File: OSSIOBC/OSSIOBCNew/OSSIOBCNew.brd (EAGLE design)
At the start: 94 x 94 mm, 158 parts, among them Q2 NX-3215, U1 PCA9548APWR, U10 MAX6369, U11 OPA4347, U13 SN65HVD11QD, U14 LTC4411, U15 MCP1700_SOT23, U16 DS3231-L, U17 FM24V02-G, U18 TMP101, U19 24LC256-8LEAD, U2 ADG708, U20 LTC4411, U21 SN74LVC8T245PWR, U23 ADXRS450SOIC, U3 MAX890L, U4 OPA4347, U5 MSP430F1611, U6 OPA4347, U7 TPS3838, U8 ADG708, U9 ADR121, X1 ESQ-126-38-G-D, X2 JTAG10PINMINI-H, X3 MOLEX-22-05-7045, X5 P-PAD-S, X6 P-PAD-S

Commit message: schematics renumbered
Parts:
- removed C42: 10uF, LDO Tantal 16V, OSSI:C1206(3216)-A
- removed U23: ADXRS450SOIC, OSSI:SOIC-16CAV
- added C35: 100nF, OSSI:C0603(1608)
- added U12: TMP101, OSSI:SOT23-6DBV
- C1: value 1uF -> 100nF
- C13, C14: value 12.5pF -> 100nF
- C20, C22, C23: value 100nF -> 1uF 0805; device OSSI:C0603(1608) -> OSSI:C0805(2012)
- C29: value 1uF 0805 -> 4.7uF, 1210; device OSSI:C0805(2012) -> OSSI:C1206-GCM31
- C30: value 1uF 0805 -> 10uF,3225; device OSSI:C0805(2012) -> OSSI:C1210-GCM32
- C31: value 100nF -> 12.5pF
- C32: value 1uF 0805 -> 12.5pF; device OSSI:C0805(2012) -> OSSI:C0603(1608)
- C34: value 10uF, LDO Tantal 16V -> 100nF; device OSSI:C1206(3216)-A -> OSSI:C0603(1608)
- C37: value 10uF,3225 -> 100nF; device OSSI:C1210-GCM32 -> OSSI:C0603(1608)
- C38: value 4.7uF, 1210 -> 1uF; device OSSI:C1206-GCM31 -> OSSI:C0603(1608)
- C40, C41: value 100nF -> 10uF, LDO Tantal 16V; device OSSI:C0603(1608) -> OSSI:C1206(3216)-A
- R1: value TBD -> 10k
- R10, R11, R62: value 10k -> 100k
- R12, R13: value 33k -> 100k
- R18, R2, R3, R4, R6, R7, R9: value 100k -> 10k
- R19, R41: value 100k -> 250
- R20, R43: value 100k -> 470k
- R21, R30, R31, R38: value 10k -> 250
- R22, R23, R26, R28, R29: value 250 -> 1.5k
- R27: value 250 -> 100k
- R32: value 250 -> 4.7k
- R33: value 250 -> 470k
- R34: value 4.7k -> 470k
- R35: value 120, DNP -> 33k
- R36, R39, R68, R71: value 10k -> 4.7k
- R37: value 10k -> 120, DNP
- R40: value 10k -> 33k
- R42, R69, R70: value 1.5k -> 4.7k
- R44: value 470k -> 4.7k
- R45: value 4.7k -> 100k
- R46: value 1.5k -> 470k
- R47, R48, R49: value 1.5k -> 100k
- R52, R57: value 4.7k -> 1.5k
- R54: value 1.5k -> 10k
- R56: value 10k -> 1.5k
- R58, R60, R65: value 470k -> 10k
- R59, R61, R8: value 4.7k -> 10k
- R63: value 4.7k -> 250
- R64: value 470k -> 250
- R66: value 4.7k -> 300k
- R67: value 300k -> 10k
- R72, R73: value 10k -> 0
- R74: value 100k -> TBD
- R76, R77: value 0 -> 100k
- U1: value PCA9548APWR -> OPA4347; device OSSI:TSSOP-24-PW -> OSSI:TSSOP14-PW
- U10: value MAX6369 -> ADXRS450SOIC; device OSSI:SOT23-8 -> OSSI:SOIC-16CAV
- U11: value OPA4347 -> FM24V02-G; device OSSI:TSSOP14-PW -> OSSI:SO8
- U14: value LTC4411 -> PCA9548APWR; device OSSI:TSOT23-5 -> OSSI:TSSOP-24-PW
- U15: value MCP1700_SOT23 -> SN74LVC8T245PWR; device OSSI:SOT23 -> OSSI:PW_R-PDSO-G24
- U16: value DS3231-L -> LTC4411; device OSSI:SO16L -> OSSI:TSOT23-5
- U17: value FM24V02-G -> MSP430F1611; device OSSI:SO8 -> OSSI:PM/PAG64
- U18: value TMP101 -> MAX6369; device OSSI:SOT23-6DBV -> OSSI:SOT23-8
- U19: value 24LC256-8LEAD -> TPS3838; device OSSI:SO08-208 -> OSSI:SOT23-5DBV
- U20: value LTC4411 -> MAX890L; device OSSI:TSOT23-5 -> OSSI:SO8
- U21: value SN74LVC8T245PWR -> MCP1700_SOT23; device OSSI:PW_R-PDSO-G24 -> OSSI:SOT23
- U3: value MAX890L -> OPA4347; device OSSI:SO8 -> OSSI:TSSOP14-PW
- U4: value OPA4347 -> ADR121; device OSSI:TSSOP14-PW -> OSSI:TSOT-6UJ-6
- U5: value MSP430F1611 -> ADG708; device OSSI:PM/PAG64 -> OSSI:TSSOP16-RU
- U7: value TPS3838 -> DS3231-L; device OSSI:SOT23-5DBV -> OSSI:SO16L
- U8: value ADG708 -> 24LC256-8LEAD; device OSSI:TSSOP16-RU -> OSSI:SO08-208
- U9: value ADR121 -> LTC4411; device OSSI:TSOT-6UJ-6 -> OSSI:TSOT23-5
- X2: value JTAG10PINMINI-H -> MOLEX-22-05-7045; device OSSI:M50-3200545 -> OSSI:22-05-7045
- X3: value MOLEX-22-05-7045 -> (none); device OSSI:22-05-7045 -> OSSI:1X03
- X4: value (none) -> P-PAD-S; device OSSI:1X03 -> OSSI:P-PAD-S
- X6: value P-PAD-S -> JTAG10PINMINI-H; device OSSI:P-PAD-S -> OSSI:M50-3200545
- moved R74 82.4 mm to (67.8, 85.0), turned to 0 degrees
- moved R20 81.5 mm to (53.3, 6.02), turned to 180 degrees
- moved U16 77.4 mm to (62.2, 90.0), turned to 270 degrees
- moved H1 76.0 mm to (85.0, 85.0)
- moved H2 76.0 mm to (85.0, 9.00)
- moved H3 76.0 mm to (9.00, 9.00)
- moved H4 76.0 mm to (9.00, 85.0)
- moved R41 73.8 mm to (29.0, 18.8), turned to 270 degrees
- moved U9 71.9 mm to (46.1, 6.50)
- moved U7 70.5 mm to (55.8, 12.9), turned to 0 degrees
- moved U19 64.0 mm to (20.5, 74.0), turned to 270 degrees
- moved R52 63.9 mm to (16.1, 54.0), flipped to the top, turned to 90 degrees
- moved C2 63.9 mm to (71.0, 52.2)
- moved R53 62.5 mm to (17.6, 52.0), flipped to the top, turned to 90 degrees
- moved R38 61.2 mm to (30.5, 17.0), turned to 270 degrees
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- renumbered Q2 to Q1, TR2 to TR1
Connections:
- net /RE: now also R40.1; no longer R12.1
- net 3.3VOBC: now also C14.2, C20.1, C26.1, C34.1, C36.1, C37.1, C4.1, C41.1, C9.1, R34.2, R40.2, R46.2, R48.2, R54.2, R59.2, R65.2, R66.1, R67.2, R77.2, U1.4, U14.24, U15.1, U17.1, U17.64, U18.4, U18.5, U18.6, U18.8, U19.5, U21.2, U3.4, U4.3, U5.13, U5.2, U9.P$1, X6.4; no longer C12.1, C17.2, C2.1, C27.1, C30.1, C42.1, C6.1, C7.1, C8.1, R12.2, R2.2, R30.2, R31.2, R4.2, R44.2, R56.2, R58.2, R67.1, R73.2, U1.24, U10.4, U10.5, U10.8, U11.4, U14.P$1, U15.2, U21.1, U23.6, U4.4, U5.1, U5.64, U7.5, U8.13, U8.2, U9.3, X2.4
- net 3.3VOBC_I2C: now also C24.1, C25.1, R20.2, R33.1, R58.2, R61.2, U11.1, U11.8, U12.4, U7.2, U8.8, U9.P$5; no longer C20.1, C21.1, R5.2, R64.2, R65.1, R72.2, U14.P$5, U16.2, U17.1, U17.8, U18.4, U19.8
- net A: now also R37.2, X2.2; no longer R35.2, X3.2
- net ADC0: now also C12.1, R9.1, U17.59; no longer C5.1, R10.1, U5.59
- net ADC1: now also C17.1, R18.1, U17.60; no longer C9.1, R11.1, U5.60
- net ANT_DEPLOY1: now also R70.1; no longer R45.1
- net ANT_DEPLOY2: now also R69.1; no longer R52.1
- net B: now also R37.1, X2.3; no longer R35.1, X3.3
- net BAT_-CHRG: now also U15.18; no longer U21.18
- net BAT_-CHRG_IN: now also R53.2, U17.17; no longer R48.2, U5.17
- net BAT_-FAULT: now also U15.17; no longer U21.17
- net BAT_-FAULT_IN: now also R52.2, U17.16; no longer R49.2, U5.16
- net BAT_-ON: now also U15.20; no longer U21.20
- net BAT_-ON_IN: now also R56.2, U17.19; no longer R46.2, U5.19
- net BAT_TEMP: now also R2.2; no longer R68.2
- net BEACON_-FAULT: now also R42.1, R43.1; no longer R58.1, R59.1
- net BEACON_-FAULT_IN: now also R42.2, U17.22; no longer R59.2, U5.22
- net BEACON_OFF: now also R28.1; no longer R54.1
- net BEACON_OFF_OUT: now also R28.2, U17.38; no longer R54.2, U5.38
- net BEACON_SCL: now also U14.7; no longer U1.7
- net BEACON_SDA: now also U14.6; no longer U1.6
- net BUS_CS: now also R4.2; no longer R40.2
- net COMMS_-FAULT: now also R32.1, R34.1; no longer R60.1, R61.1
- net COMMS_-FAULT_IN: now also R32.2, U17.21; no longer R61.2, U5.21
- net COMMS_OFF: now also R26.1; no longer R55.1
- net COMMS_OFF_OUT: now also R26.2, U17.37; no longer R55.2, U5.37
- net COMMS_SCL: now also U14.5; no longer U1.5
- net COMMS_SDA: now also U14.4; no longer U1.4
- net DE: now also R35.2, U17.48; no longer R13.2, U5.48
- net GND: now also C13.1, C14.1, C17.2, C21.1, C29.P$2, C30.P$2, C31.2, C33.2, C35.2, C37.2, C38.2, R10.1, R12.1, R14.1, R16.1, R27.2, R35.1, R45.2, R49.2, R74.1, R76.1, U1.11, U10.10, U10.11, U10.12, U10.13, U10.3, U10.7, U11.2, U11.3, U11.4, U11.7, U12.2, U12.5, U14.1, U14.12, U14.2, U14.21, U15.11, U15.12, U15.13, U15.14, U15.2, U16.P$2, U17.11, U17.53, U17.62, U17.63, U20.4, U21.1, U3.11, U4.2, U5.10, U5.12, U5.14, U5.3, U5.9, U7.10, U7.11, U7.12, U7.13, U7.5, U7.6, U7.7, U7.8, U7.9, U8.1, U8.2, U8.4, U8.7, U9.P$2, X2.4, X3.3, X6.9; no longer C13.2, C14.2, C17.1, C21.2, C29.2, C30.2, C31.1, C33.1, C37.P$2, C38.P$2, C41.2, R1.1, R13.1, R15.1, R17.1, R19.1, R20.2, R3.1, R41.2, R74.2, R9.1, U1.1, U1.12, U1.2, U1.21, U11.11, U14.P$2, U15.1, U16.10, U16.11, U16.12, U16.13, U16.5, U16.6, U16.7, U16.8, U16.9, U17.2, U17.3, U17.4, U17.7, U18.5, U19.3, U19.4, U19.7, U2.10, U2.11, U2.12, U2.9, U20.P$2, U21.11, U21.12, U21.13, U21.14, U21.2, U23.10, U23.11, U23.12, U23.13, U23.2, U23.3, U23.7, U3.4, U4.11, U5.53, U5.62, U5.63, U7.1, U7.2, U8.14, U9.2, X2.9, X3.4, X4.3
- net GYRO_-CS: now also U10.4, U17.44; no longer U23.4, U5.44
- net GYRO_SCLK: now also U10.16, U17.47; no longer U23.16, U5.47
- net GYRO_SI: now also U10.15, U17.45; no longer U23.15, U5.45
- net GYRO_SO: now also U10.5, U17.46; no longer U23.5, U5.46
- net I2C_-RST: now also R48.1, U14.3, U17.28; no longer R4.1, U1.3, U5.28
- net I2C_SCL: now also R64.1, R67.1, U14.22; no longer R26.1, R30.1, U1.22
- net I2C_SCL_TP: now also R64.2, U17.31, X3.2; no longer R26.2, U5.31, X4.2
- net I2C_SDA: now also R63.1, R65.1, U14.23; no longer R27.1, R31.1, U1.23
- net I2C_SDA_TP: now also R63.2, U17.29, X3.1; no longer R27.2, U5.29, X4.1
- net IO_-OE: now also R62.1, U15.22, U17.24; no longer R43.1, U21.22, U5.24
- net LED_-FAULT: now also R46.1; no longer R57.1
- net LED_-FAULT_IN: now also R44.2, U17.23; no longer R57.2, U5.23
- net LED_OFF: now also R29.1; no longer R53.1
- net LED_OFF_OUT: now also R29.2, U17.39; no longer R53.2, U5.39
- net LED_SCL: now also U14.9; no longer U1.9
- net LED_SDA: now also U14.8; no longer U1.8
- net MUX_A0: now also R73.2, U5.1; no longer R76.2, U8.1
- net MUX_A1: now also R72.2, U5.16; no longer R77.2, U8.16
- net MUX_A2: now also U17.51, U5.15; no longer U5.51, U8.15
- net N$1: now also U17.12, U18.1; no longer U10.1, U5.12
- net N$10: now also R74.2, U20.5; no longer R1.2, U3.5
- net N$11: now also U5.4, U6.13, U6.14; no longer U2.4, U4.13, U4.14
- net N$12: now also U2.7, U3.1, U3.2; no longer U6.1, U6.2, U8.7
- net N$13: now also C33.1, U17.7; no longer C10.1, U5.7
- net N$14: now also R39.2; no longer R34.2
- net N$15: now also R21.2, U7.16; no longer R33.2, U16.16
- net N$16: now also R54.1, U14.15, U14.16, U14.17, U14.18, U14.19, U14.20; no longer R73.1, U1.15, U1.16, U1.17, U1.18, U1.19, U1.20
- net N$17: now also U17.57, X6.7; no longer U5.57, X2.7
- net N$18: now also U17.56, X6.5; no longer U5.56, X2.5
- net N$19: now also U17.55, X6.3; no longer U5.55, X2.3
- net N$2: now also R16.2, R17.1, U6.3; no longer R7.1, R9.2, U4.3
- net N$20: now also U17.54, X6.1; no longer U5.54, X2.1
- net N$21: now also U2.6, U3.6, U3.7; no longer U6.6, U6.7, U8.6
- net N$22: now also R36.2; no longer R63.2
- net N$23: now also R71.1, X6.10; no longer R8.1, X2.10
- net N$24: now also R14.2, R15.1, U6.5; no longer R14.1, R15.2, U4.5
- net N$25: now also R12.2, R13.1, U6.10; no longer R16.1, R17.2, U4.10
- net N$26: now also R10.2, R11.1, U6.12; no longer R18.1, R19.2, U4.12
- net N$27: now also R18.2, U5.8; no longer R11.2, U2.8
- net N$28: now also U2.5, U3.8, U3.9; no longer U6.8, U6.9, U8.5
- net N$29: now also R9.2, U2.8; no longer R10.2, U8.8
- net N$3: now also U5.7, U6.1, U6.2; no longer U2.7, U4.1, U4.2
- net N$30: now also U2.4, U3.13, U3.14; no longer U6.13, U6.14, U8.4
- net N$31: now also U1.1, U1.2, U2.12; no longer U11.1, U11.2, U8.12
- net N$32: now also R68.2, U17.13; no longer R66.2, U5.13
- net N$33: now also C23.1, U10.1; no longer C32.1, U23.1
- net N$34: now also R24.2, U8.5; no longer R29.2, U19.5
- net N$35: now also R25.2, U8.6; no longer R28.2, U19.6
- net N$36: now also R30.2, U11.5; no longer R25.2, U17.5
- net N$37: now also R70.2, U17.43; no longer R45.2, U5.43
- net N$38: now also R69.2, U17.42; no longer R52.2, U5.42
- net N$39: now also R31.2, U11.6; no longer R24.2, U17.6
- net N$4: now also R45.1, R47.2; no longer R41.1, R6.2
- net N$40: now also R38.2, U12.6; no longer R22.2, U18.6
- net N$41: now also R41.2, U12.1; no longer R23.2, U18.1
- net N$42: now also R66.2, U17.25; no longer R67.2, U5.25
- net N$43: now also C27.1, X2.1; no longer C36.1, X3.1
- net N$44: now also U1.8, U1.9, U2.10; no longer U11.8, U11.9, U8.10
- net N$45: now also U1.13, U1.14, U2.9; no longer U11.13, U11.14, U8.9
- net N$46: now also C22.1, U10.14; no longer C29.1, U23.14
- net N$47: now also C1.1, R1.1, U1.12; no longer C41.1, R71.1, U11.12
- net N$48: now also C2.1, R2.1, U1.10; no longer C40.1, R68.1, U11.10
- net N$49: now also R53.1, U15.6; no longer R48.1, U21.6
- net N$5: now also C32.1, U17.8; no longer C13.1, U5.8
- net N$50: now also R52.1, U15.7; no longer R49.1, U21.7
- net N$51: now also C10.1, R8.1, U3.3; no longer C22.1, R21.1, U6.3
- net N$52: now also C8.1, R7.1, U3.5; no longer C23.1, R36.1, U6.5
- net N$53: now also C7.1, R6.1, U3.10; no longer C24.1, R37.1, U6.10
- net N$54: now also C6.1, R5.1, U3.12; no longer C25.1, R38.1, U6.12
- net N$55: now also C3.1, R3.1, U1.3; no longer C26.1, R39.1, U11.3
- net N$56: now also R51.1, U15.8; no longer R50.1, U21.8
- net N$57: now also R50.1, U15.9; no longer R51.1, U21.9
- net N$58: now also C5.1, R4.1, U1.5; no longer C39.1, R40.1, U11.5
- net N$59: now also C41.2; no longer C42.2
- net N$6: now also C31.1, U17.9; no longer C14.1, U5.9
- net N$60: now also U17.33; no longer U5.33
- net N$61: now also U17.32, X4.1; no longer U5.32, X6.1
- net N$62: now also R73.1, U17.49; no longer R76.1, U5.49
- net N$64: now also R72.1, U17.50; no longer R77.1, U5.50
- net N$65: now also U7.14; no longer U16.14
- net N$666: now also C39.1, C40.1, U20.6, U20.7, U21.3; no longer C3.1, C34.1, U15.3, U3.6, U3.7
- net N$7: now also R19.2, U7.15; no longer R32.2, U16.15
- net N$70: now also R55.1, U15.5; no longer R47.1, U21.5
- net N$71: now also R56.1, U15.4; no longer R46.1, U21.4
- net N$72: now also R57.1, U15.3; no longer R42.1, U21.3
- net N$8: now also U5.6, U6.6, U6.7; no longer U2.6, U4.6, U4.7
- net N$82: now also U10.8; no longer U23.8
- net N$9: now also U5.5, U6.8, U6.9; no longer U2.5, U4.8, U4.9
- net N$90: now also C21.2, U10.9; no longer C31.2, U23.9
- net OBC_-FAULT: now also U20.8; no longer U3.8
- net OBC_I2C_OFF: now also R27.1, U17.30, U9.P$3; no longer R74.1, U14.P$3, U5.30
- net OBC_OFF: now also C38.1, R76.2, U20.3; no longer C1.1, R3.2, U3.3
- net OBC_SCL: now also R21.1, R25.1, R31.1, R41.1, R58.1, U14.14; no longer R23.1, R24.1, R28.1, R33.1, R72.1, U1.14
- net OBC_SDA: now also R19.1, R24.1, R30.1, R38.1, R61.1, U14.13; no longer R22.1, R25.1, R29.1, R32.1, R5.1, U1.13
- net OBC_WT_RST: now also C35.1, U18.7, U19.3; no longer C4.1, U10.7, U7.3
- net PANELTEMP_SCL: now also R59.1, U14.11; no longer R56.1, U1.11
- net PANELTEMP_SDA: now also R60.1, U14.10; no longer R62.1, U1.10
- net RESETOBC: now also R71.2, R77.1, U17.58, U19.4; no longer R2.1, R8.2, U5.58, U7.4
- net RTC_-INT: now also R20.1, U17.26, U7.3; no longer R64.1, U16.3, U5.26
- net RXD1: now also R39.1, U17.35; no longer R34.1, U5.35
- net SCCHG_EN: now also R23.1; no longer R69.1
- net SCCHG_EN_OUT: now also R23.2, U17.41; no longer R69.2, U5.41
- net SCOUT_-PG: now also U15.15; no longer U21.15
- net SCOUT_-PG_IN: now also R50.2, U17.14; no longer R51.2, U5.14
- net SCOUT_EN: now also R22.1; no longer R70.1
- net SCOUT_EN_OUT: now also R22.2, U17.40; no longer R70.2, U5.40
- net SC_-ON: now also U15.19; no longer U21.19
- net SC_-ON_IN: now also R55.2, U17.18; no longer R47.2, U5.18
- net SC_-PFO: now also U15.16; no longer U21.16
- net SC_-PFO_IN: now also R51.2, U17.15; no longer R50.2, U5.15
- net SOLAR_-ON: now also U15.21; no longer U21.21
- net SOLAR_-ON_IN: now also R57.2, U17.20; no longer R42.2, U5.20
- net SOLAR_CS1: now also R8.2; no longer R21.2
- net SOLAR_CS2: now also R7.2; no longer R36.2
- net SOLAR_CS3: now also R6.2; no longer R37.2
- net SOLAR_CS4: now also R5.2; no longer R38.2
- net SOLAR_CS5: now also R3.2; no longer R39.2
- net STATUS_LED: now also R68.1; no longer R66.1
- net SUN_IN: now also U1.6, U1.7, U2.11; no longer U11.6, U11.7, U8.11
- net SUPERCAP_TEMP: now also R1.2; no longer R71.2
- net TEMP_-ALERT: now also R33.2, U12.3, U17.27; no longer R65.2, U18.3, U5.27
- net TXD1: now also R36.1, U17.34; no longer R63.1, U5.34
- net VBAT: now also R13.2; no longer R16.2
- net VBUS: now also R15.2, U15.23, U15.24, U20.1, U20.2; no longer R14.2, U21.23, U21.24, U3.1, U3.2
- net VEXT: now also C30.P$1, R47.1, U16.P$1; no longer C37.P$1, R6.1, U20.P$1
- net VEXT_OFF: now also R49.1, U16.P$3, U17.36; no longer R20.1, U20.P$3, U5.36
- net VREF_EXT: now also C13.2, U17.10, U4.4; no longer C33.2, U5.10, U9.4
- net VSOLAR: now also C29.P$1, R17.2, U16.P$5; no longer C38.P$1, R7.2, U20.P$5
- net VSUPERCAP: now also R11.2; no longer R18.2

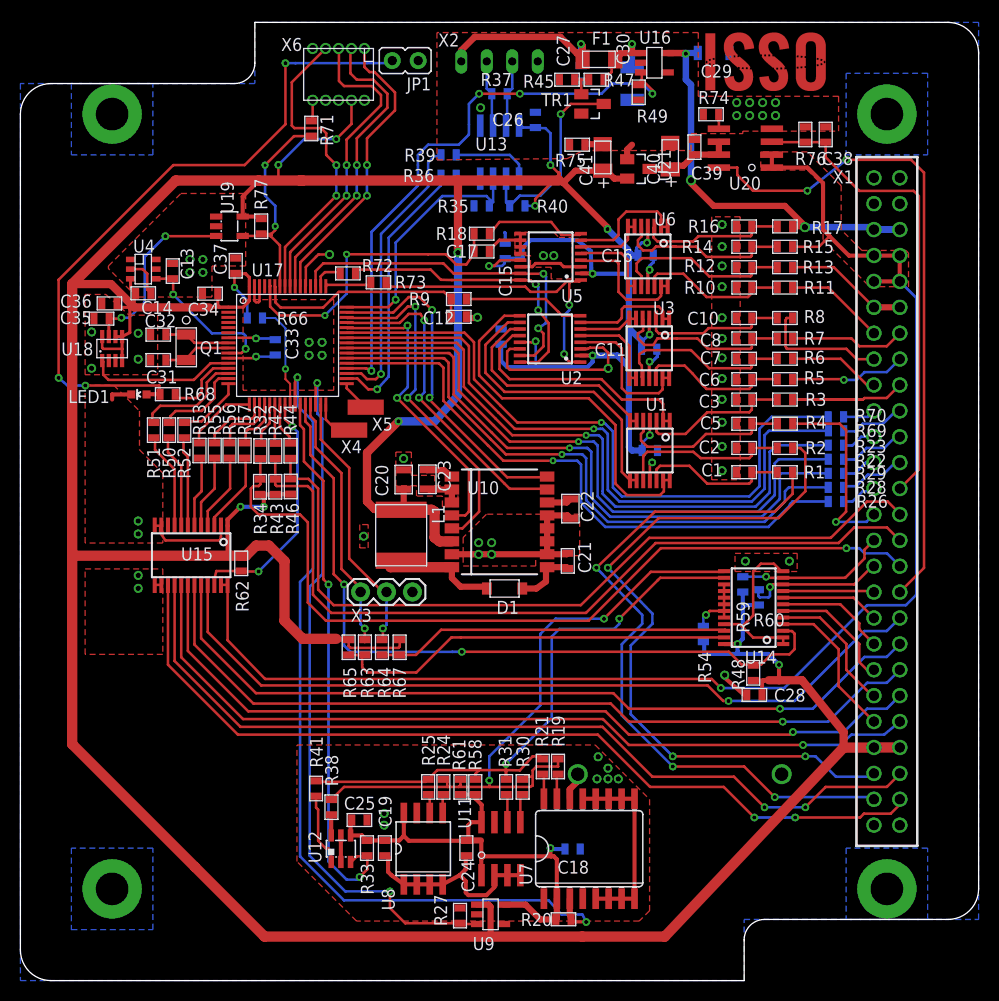
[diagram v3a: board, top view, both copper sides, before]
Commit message: OBC renumbered
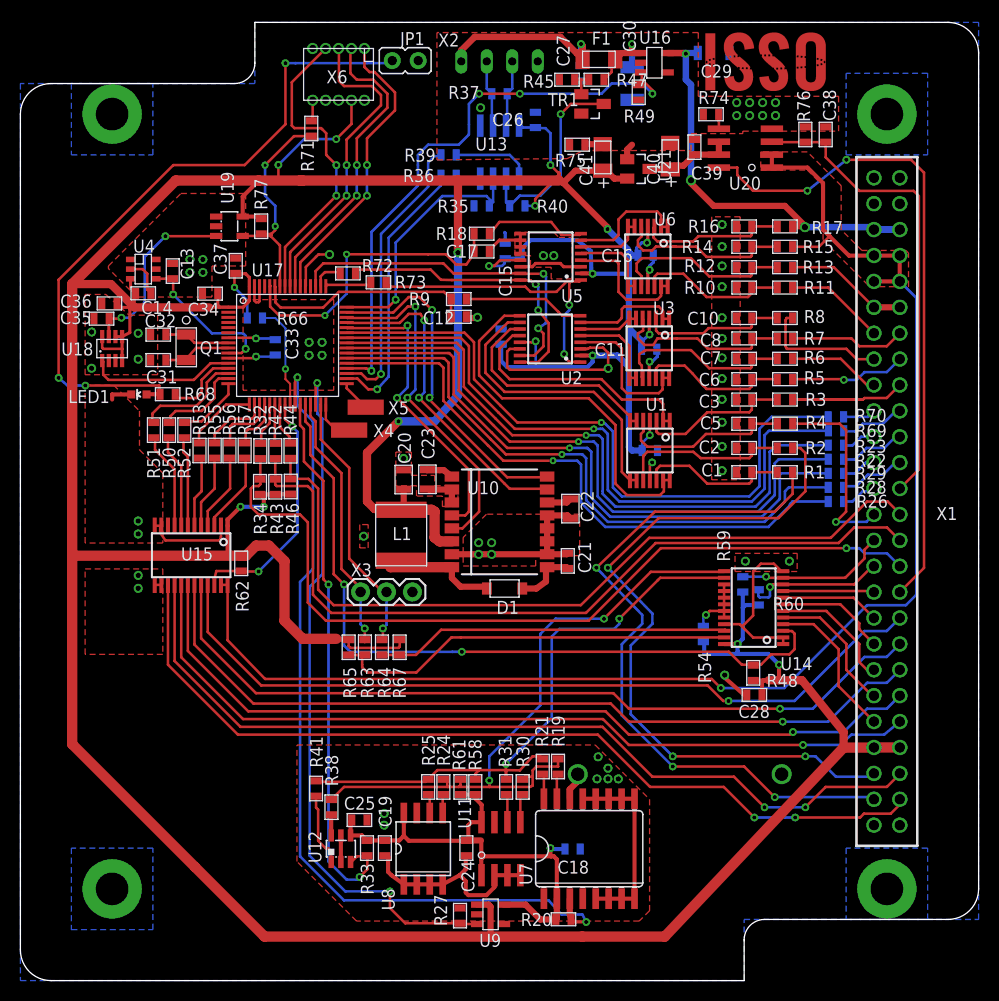
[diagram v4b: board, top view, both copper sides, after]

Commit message: all values for tuned results are updated
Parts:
- R74: value TBD -> 6.2k
- U14: value PCA9548APWR -> TCA9548APWR
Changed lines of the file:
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@@
 <attribute name="VALUE" x="73.3425" y="85.7875" size="1.27" layer="27" rot="R180"/>
 </element>
-<element name="R74" library="OSSI" package="R0603(1608)" value="TBD" x="67.75" y="84.984" smashed="yes">
+<element name="R74" library="OSSI" package="R0603(1608)" value="6.2k" x="67.75" y="84.984" smashed="yes">
 <attribute name="NAME" x="66.486" y="85.998" size="1.27" layer="25" font="vector"/>
 <attribute name="VALUE" x="66.861" y="82.952" size="1.27" layer="27"/>
@@
 <attribute name="VALUE" x="42.111" y="63.083" size="1.27" layer="27"/>
 </element>
-<element name="U14" library="OSSI" package="TSSOP-24-PW" value="PCA9548APWR" x="71.93" y="36.59" smashed="yes" rot="R90">
+<element name="U14" library="OSSI" package="TSSOP-24-PW" value="TCA9548APWR" x="71.93" y="36.59" smashed="yes" rot="R90">
 <attribute name="NAME" x="77.6975" y="31.73" size="1.27" layer="25" font="vector" rot="R180"/>
 <attribute name="VALUE" x="74.205" y="42.115" size="1.27" layer="27" rot="R180"/>
